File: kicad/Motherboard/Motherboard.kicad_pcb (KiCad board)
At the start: 2 copper layers, 72.1 x 0.1 mm, 68 parts, among them J1 USB_C_Receptacle_USB2.0, J10 Conn_01x08_Pin, J11 Conn_01x08_Pin, J12 Conn_01x08_Pin, J13 Conn_01x08_Pin, J2 Conn_01x02_Pin, J3 Conn_01x04_Pin, J4 Conn_01x04_Pin, J5 Conn_01x02_Pin, J6 Conn_01x08_Pin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

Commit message: Layout work
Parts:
- moved J8 96.0 mm to (154.9, 93.8), turned to -90 degrees
- moved J4 86.1 mm to (130.0, 129.8), turned to -90 degrees
- moved J10 84.0 mm to (86.2, 80.1), turned to 90 degrees
- moved J3 80.9 mm to (117.2, 129.8), turned to -90 degrees
- moved TP3 72.8 mm to (138.2, 107.6), turned to 180 degrees
- moved J5 66.6 mm to (90.0, 128.1), turned to -90 degrees
- moved J1 64.7 mm to (88.2, 119.8), turned to -90 degrees
- moved J2 56.5 mm to (103.7, 121.7), turned to 180 degrees
- moved Q1 56.4 mm to (95.7, 128.3), turned to 180 degrees
- moved J9 52.3 mm to (137.1, 80.0), turned to 90 degrees
- moved U6 50.6 mm to (144.4, 105.8), turned to 90 degrees
- moved R4 50.5 mm to (99.1, 128.1), turned to -90 degrees
- moved R1 50.3 mm to (96.0, 121.5), turned to 180 degrees
- moved R3 48.8 mm to (96.0, 118.5), turned to 0 degrees
- moved R5 42.8 mm to (103.9, 127.1), turned to 180 degrees
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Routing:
- net +3.3V: track 0.00 -> 55.6 mm
- net VS_1: track 0.00 -> 51.8 mm, vias 0 -> 2
- net Net-(U1-EN): track 0.00 -> 27.5 mm
- net Net-(J11-Pin_1): track 0.00 -> 10.7 mm
- net Net-(J11-Pin_8): track 0.00 -> 10.6 mm
- net Net-(J10-Pin_8): track 0.00 -> 9.72 mm
- net Net-(J10-Pin_1): track 0.00 -> 9.33 mm
- net Net-(J11-Pin_7): track 0.00 -> 8.74 mm
- net Net-(J11-Pin_2): track 0.00 -> 8.65 mm
- net Net-(J10-Pin_7): track 0.00 -> 8.04 mm
- net Net-(J10-Pin_2): track 0.00 -> 7.27 mm
- net Net-(J11-Pin_3): track 0.00 -> 7.10 mm
- net Net-(J11-Pin_6): track 0.00 -> 6.91 mm
- net Net-(J10-Pin_6): track 0.00 -> 6.30 mm
- net Net-(J11-Pin_4): track 0.00 -> 6.26 mm
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- added copper zone on B.Cu, net GND
- added copper zone on F.Cu, net GND
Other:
- board size 72.1 x 0.1 mm -> 72.6 x 54.1 mm

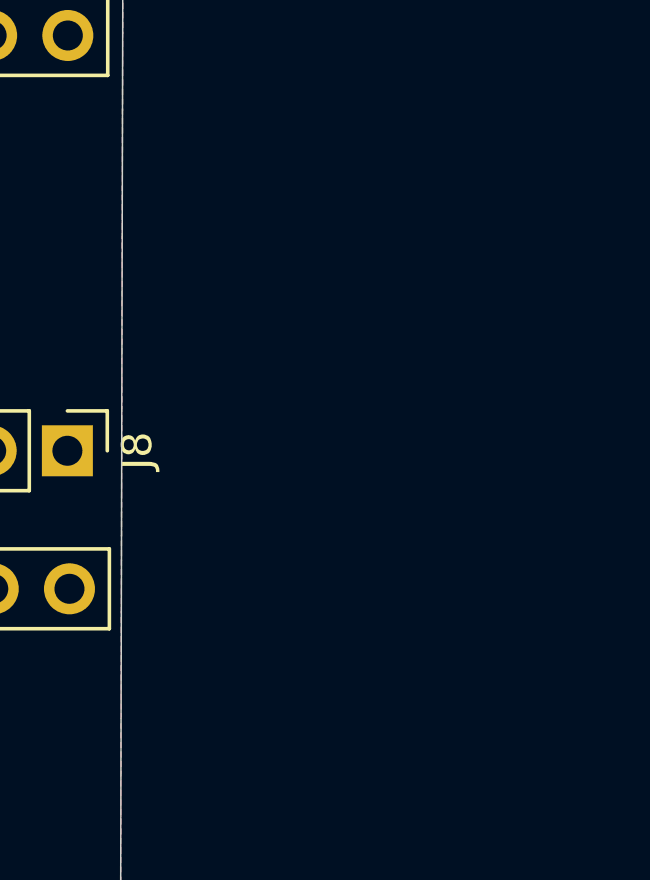
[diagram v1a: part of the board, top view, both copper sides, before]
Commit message: finalized schematic
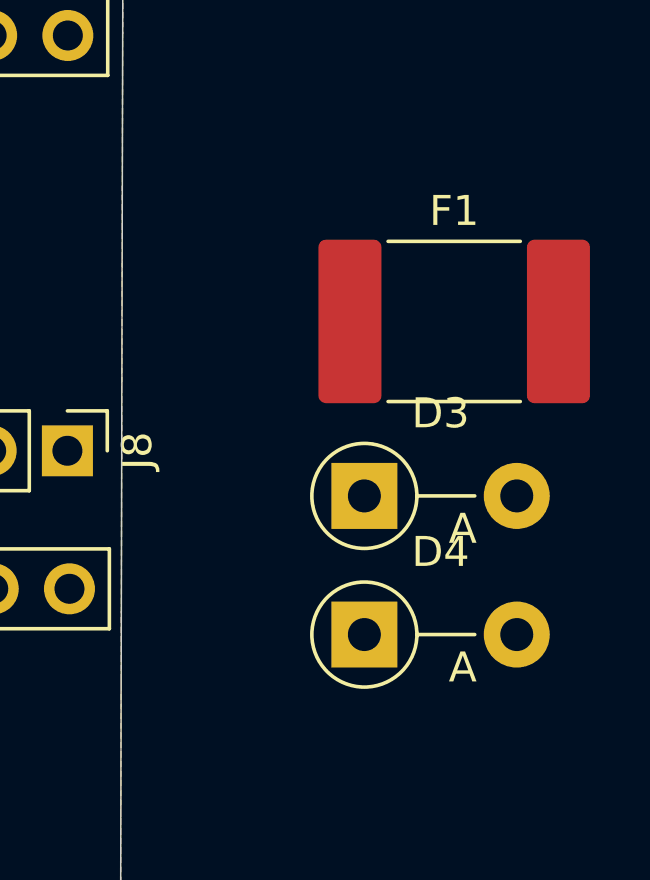
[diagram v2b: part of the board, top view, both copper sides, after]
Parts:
- added D3: 1N5819, Diode_THT:D_DO-41_SOD81_P5.08mm_Vertical_AnodeUp, F.Cu at (164.8, 95.3)
- added D4: 1N5819, Diode_THT:D_DO-41_SOD81_P5.08mm_Vertical_AnodeUp, F.Cu at (164.8, 100.0)
- added F1: Polyfuse, Fuse:Fuse_2920_7451Metric_Pad2.10x5.45mm_HandSolder, F.Cu at (167.8, 89.5)
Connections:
- C8 pad 1: +5V -> Net-(D4-A)
- J1 pad A4: +5V -> Net-(D3-A)
- J1 pad A9: +5V -> Net-(D3-A)
- J1 pad B4: +5V -> Net-(D3-A)
- J1 pad B9: +5V -> Net-(D3-A)
- L1 pad 2: +5V -> Net-(D4-A)
- TP2 pad 1: +5V -> Net-(D4-A)

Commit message: finish pls sia
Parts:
- moved F1 80.6 mm to (89.5, 108.8)
- moved D3 69.0 mm to (99.9, 119.1), turned to -90 degrees
- moved D4 62.0 mm to (107.6, 124.0), turned to 90 degrees
- moved TP4 16.2 mm to (135.6, 118.6)
- moved J5 13.6 mm to (89.8, 114.6), turned to 90 degrees
- moved C3 13.3 mm to (99.7, 105.7), turned to 0 degrees
- moved L1 12.3 mm to (87.8, 97.9), turned to 0 degrees
- moved TP2 9.88 mm to (104.4, 114.9)
- moved U9 8.39 mm to (86.9, 103.6), turned to 0 degrees
- moved TP1 8.27 mm to (86.4, 113.5)
- moved R5 7.81 mm to (96.4, 129.3)
- moved J2 6.80 mm to (105.3, 128.3), turned to 90 degrees
- moved Q1 4.99 mm to (100.7, 128.3), turned to 0 degrees
- moved C8 4.68 mm to (93.8, 97.9)
- moved D2 3.84 mm to (103.8, 119.1)
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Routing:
- net +3.3V: track 55.6 -> 0.00 mm
- net +5V: track 0.00 -> 45.6 mm
- net Net-(U1-EN): track 27.5 -> 0.00 mm
- net Net-(J11-Pin_1): track 10.7 -> 0.00 mm
- net Net-(J11-Pin_8): track 10.6 -> 0.00 mm
- net Net-(J10-Pin_8): track 9.72 -> 0.00 mm
- net Net-(J10-Pin_1): track 9.33 -> 0.00 mm
- net Net-(J11-Pin_7): track 8.74 -> 0.00 mm
- net Net-(J5-Pin_1): track 0.00 -> 8.67 mm
- net Net-(J11-Pin_2): track 8.65 -> 0.00 mm
- net Net-(J10-Pin_7): track 8.04 -> 0.00 mm
- net Net-(J10-Pin_2): track 7.27 -> 0.00 mm
- net Net-(J11-Pin_3): track 7.10 -> 0.00 mm
- net Net-(J11-Pin_6): track 6.91 -> 0.00 mm
- net Net-(J10-Pin_6): track 6.30 -> 0.00 mm
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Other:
- board size 72.6 x 54.1 mm -> 73 x 52.6 mm

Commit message: finalized schematic
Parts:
- added D5: 1N5819, Diode_THT:D_DO-41_SOD81_P5.08mm_Vertical_AnodeUp, F.Cu at (161.4, 104.5)
- U7, U8: value TMC2208-LA -> TMC2209-LA
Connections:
- F1 pad 2: VS_1 -> Net-(D5-A)
- TP2 pad 1: Net-(D4-A) -> +5V

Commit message: Separated parts
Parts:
- moved D5 103.0 mm to (62.5, 133.5), turned to 90 degrees
- moved TP3 58.4 mm to (195.8, 97.3)
- moved J8 48.2 mm to (200.7, 78.2)
- moved J9 48.2 mm to (182.9, 65.0)
- moved U4 48.2 mm to (190.3, 71.4)
- moved J7 46.5 mm to (183.1, 120.9)
- moved U3 46.5 mm to (190.1, 127.9)
- moved J6 46.5 mm to (200.7, 133.8)
- moved J10 46.4 mm to (43.4, 62.1)
- moved J11 46.4 mm to (61.1, 75.9)
- moved R2 46.4 mm to (62.7, 71.9)
- moved SW1 46.4 mm to (62.7, 67.1)
- moved U5 46.4 mm to (52.2, 68.9)
- moved U6 45.8 mm to (190.0, 100.0)
- moved J12 45.8 mm to (200.3, 106.4)
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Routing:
- net VS_1: track 54.8 -> 0.00 mm, vias 2 -> 0
- net +5V: track 45.6 -> 0.00 mm
- net Net-(J5-Pin_1): track 8.67 -> 0.00 mm
- removed copper zone on B.Cu, net GND
- removed copper zone on F.Cu, net GND
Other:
- board outline removed

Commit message: sai please
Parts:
- moved TP5 75.2 mm to (149.7, 154.3)
- moved SW1 47.1 mm to (107.8, 80.6), turned to -90 degrees
- moved L1 29.3 mm to (77.4, 129.9)
- moved C8 26.5 mm to (82.3, 126.7)
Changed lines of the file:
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@@
 	(footprint "Capacitor_SMD:C_1210_3225Metric_Pad1.33x2.70mm_HandSolder"
 		(layer "F.Cu")
-		(at 60.1595 112.141)
+		(at 82.296 126.746)
 		(descr "Capacitor SMD 1210 (3225 Metric), square (rectangular) end terminal, IPC_7351 nominal with elongated pad for handsoldering. (Body size source: IPC-SM-782 page 76, https://www.pcb-3d.com/wordpress/wp-content/uploads/ipc-sm-782a_amendment_1_and_2.pdf), generated with kicad-footprint-generator")
 		(tags "capacitor handsolder")
@@
 	(footprint "Button_Switch_SMD:SW_Push_SPST_NO_Alps_SKRK"
 		(layer "F.Cu")
-		(at 62.6575 67.0925)
+		(at 107.823 80.577 -90)
 		(descr "http://www.alps.com/prod/info/E/HTML/Tact/SurfaceMount/SKRK/SKRKAHE020.html")
 		(tags "SMD SMT button")
 		(property "Reference" "SW1"
-			(at 0 -2.25 0)
+			(at 0 -2.25 90)
 			(layer "F.SilkS")
 			(effects
@@
 		)
 		(property "Value" "Reset"
-			(at 0 2.5 0)
+			(at 0 2.5 90)
 			(layer "F.Fab")
 			(effects
@@
 		)
 		(property "Footprint" "Button_Switch_SMD:SW_Push_SPST_NO_Alps_SKRK"
-			(at 0 0 0)
+			(at 0 0 -90)
 			(unlocked yes)
 			(layer "F.Fab")
@@
 		)
 		(property "Datasheet" "https://omronfs.omron.com/en_US/ecb/products/pdf/en-b3fs.pdf"
-			(at 0 0 0)
+			(at 0 0 -90)
 			(unlocked yes)
 			(layer "F.Fab")
@@
 		)
 		(property "Description" ""
-			(at 0 0 0)
+			(at 0 0 -90)
 			(unlocked yes)
 			(layer "F.Fab")
@@
 		(attr smd)
 		(fp_line
-			(start -2.07 -1.57)
-			(end 2.07 -1.57)
+			(start -2.07 1.57)
+			(end -2.07 1.27)
 			(stroke
 				(width 0.12)
@@
 		)
 		(fp_line
-			(start -2.07 -1.27)
-			(end -2.07 -1.57)
+			(start 2.07 1.57)
+			(end -2.07 1.57)
 			(stroke
 				(width 0.12)
@@
 		)
 		(fp_line
-			(start -2.07 1.57)
-			(end -2.07 1.27)
+			(start 2.07 1.27)
+			(end 2.07 1.57)
 			(stroke
 				(width 0.12)
@@
 		)
 		(fp_line
-			(start 2.07 -1.57)
-			(end 2.07 -1.27)
+			(start -2.07 -1.27)
+			(end -2.07 -1.57)
 			(stroke
 				(width 0.12)
@@
 		)
 		(fp_line
-			(start 2.07 1.27)
-			(end 2.07 1.57)
+			(start -2.07 -1.57)
+			(end 2.07 -1.57)
 			(stroke
 				(width 0.12)
@@
 		)
 		(fp_line
-			(start 2.07 1.57)
-			(end -2.07 1.57)
+			(start 2.07 -1.57)
+			(end 2.07 -1.27)
 			(stroke
 				(width 0.12)
@@
 		)
 		(fp_line
-			(start -2.75 -1.7)
-			(end 2.75 -1.7)
+			(start -2.75 1.7)
+			(end -2.75 -1.7)
 			(stroke
 				(width 0.05)
@@
 		)
 		(fp_line
-			(start -2.75 1.7)
-			(end -2.75 -1.7)
+			(start 2.75 1.7)
+			(end -2.75 1.7)
 			(stroke
 				(width 0.05)
@@
 		)
 		(fp_line
-			(start 2.75 -1.7)
-			(end 2.75 1.7)
+			(start -2.75 -1.7)
+			(end 2.75 -1.7)
 			(stroke
 				(width 0.05)
@@
 		)
 		(fp_line
-			(start 2.75 1.7)
-			(end -2.75 1.7)
+			(start 2.75 -1.7)
+			(end 2.75 1.7)
 			(stroke
 				(width 0.05)
@@
 		)
 		(fp_line
-			(start -1.95 -1.45)
-			(end 1.95 -1.45)
+			(start -1.95 1.45)
+			(end -1.95 -1.45)
 			(stroke
 				(width 0.1)
@@
 		)
 		(fp_line
-			(start -1.95 1.45)
-			(end -1.95 -1.45)
+			(start 1.95 1.45)
+			(end -1.95 1.45)
 			(stroke
 				(width 0.1)
@@
 		)
 		(fp_line
-			(start 1.95 -1.45)
-			(end 1.95 1.45)
+			(start -1.95 -1.45)
+			(end 1.95 -1.45)
 			(stroke
 				(width 0.1)
@@
 		)
 		(fp_line
-			(start 1.95 1.45)
-			(end -1.95 1.45)
+			(start 1.95 -1.45)
+			(end 1.95 1.45)
 			(stroke
 				(width 0.1)
@@
 		)
 		(fp_text user "${REFERENCE}"
-			(at 0 0 0)
+			(at 0 0 90)
 			(layer "F.Fab")
 			(effects
@@
 		)
 		(pad "1" smd roundrect
-			(at -2.1 0)
+			(at -2.1 0 270)
 			(size 0.8 2)
 			(layers "F.Cu" "F.Paste" "F.Mask")
@@
 		)
 		(pad "2" smd roundrect
-			(at 2.1 0)
+			(at 2.1 0 270)
 			(size 0.8 2)
 			(layers "F.Cu" "F.Paste" "F.Mask")
@@
 	(footprint "Inductor_SMD:L_1008_2520Metric_Pad1.43x2.20mm_HandSolder"
 		(layer "F.Cu")
-		(at 54.1215 112.141)
+		(at 77.3625 129.921)
 		(descr "Inductor SMD 1008 (2520 Metric), square (rectangular) end terminal, IPC_7351 nominal with elongated pad for handsoldering. (Body size source: https://ecsxtal.com/store/pdf/ECS-MPI2520-SMD-POWER-INDUCTOR.pdf), generated with kicad-footprint-generator")
 		(tags "inductor handsolder")
@@
 	(footprint "TestPoint:TestPoint_Pad_1.5x1.5mm"
 		(layer "F.Cu")
-		(at 132.334 81.153)
+		(at 149.733 154.305)
 		(descr "SMD rectangular pad as test Point, square 1.5mm side length")
 		(tags "test point SMD pad rectangle square")

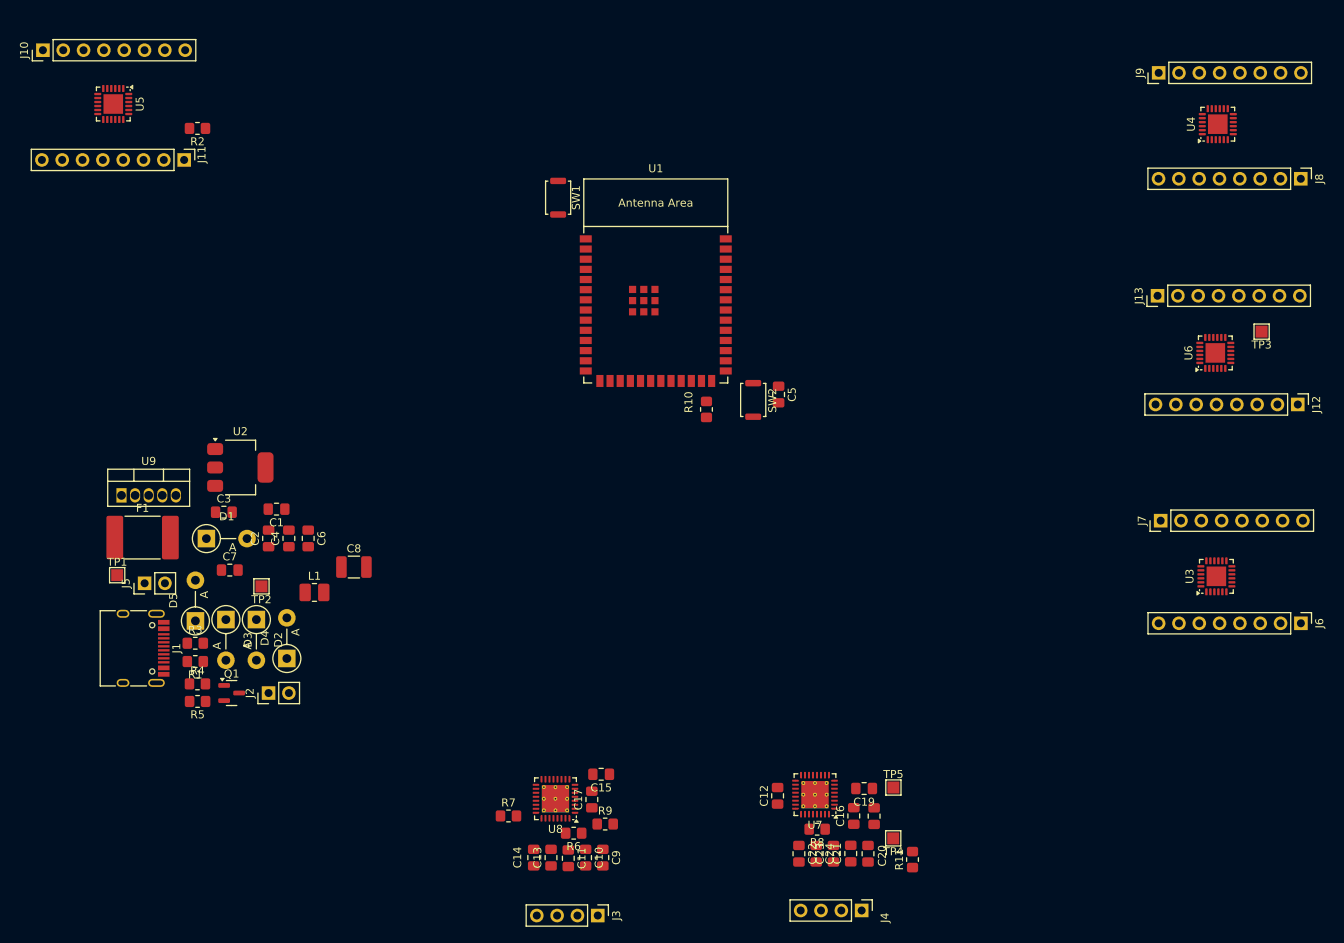
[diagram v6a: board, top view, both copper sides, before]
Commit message: updated layout
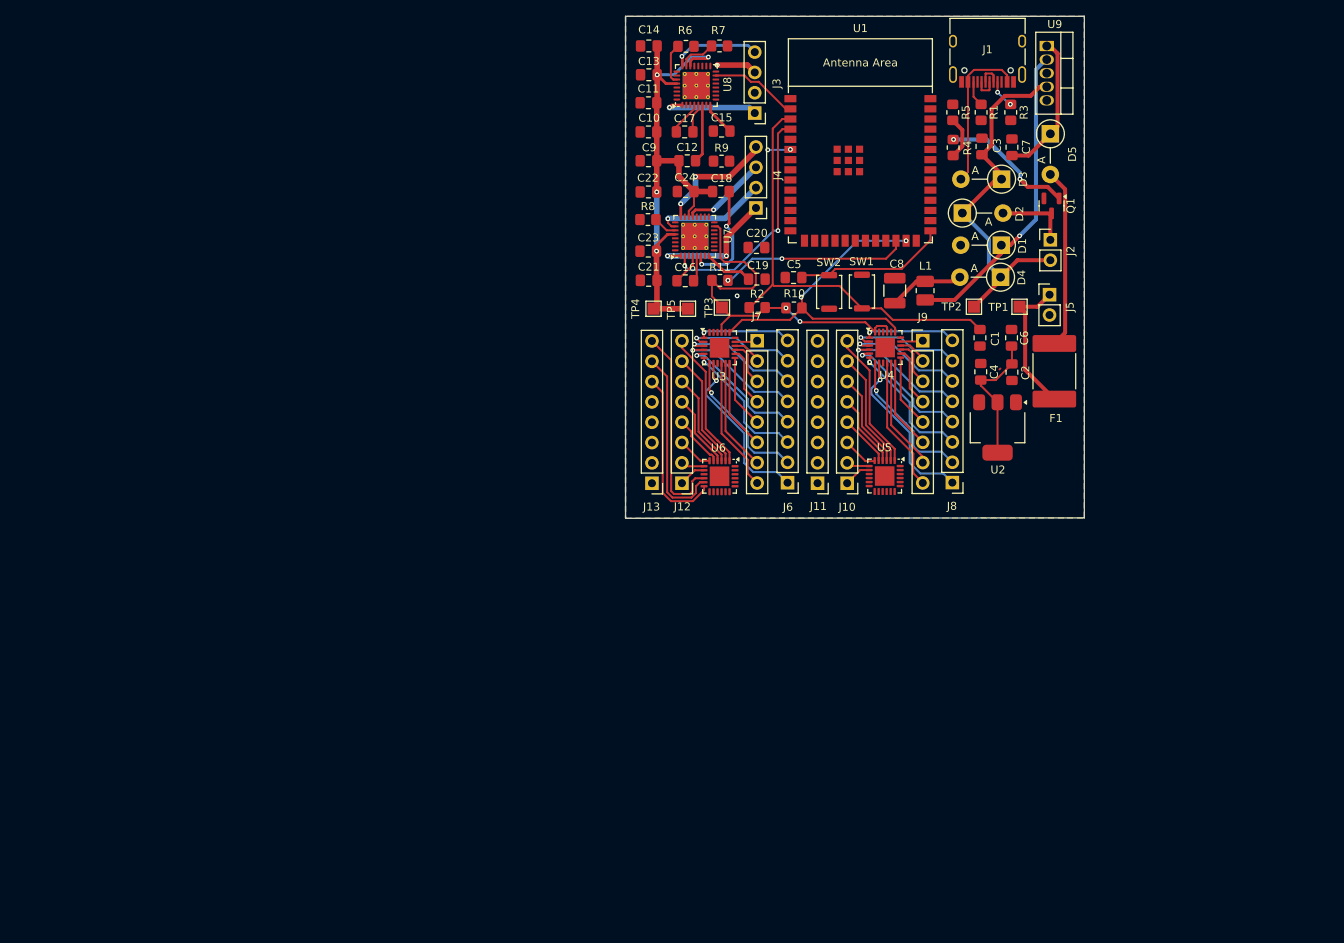
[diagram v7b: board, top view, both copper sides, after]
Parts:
- moved J1 130.6 mm to (161.5, 62.1), turned to 180 degrees
- moved U9 128.6 mm to (168.9, 61.6), turned to -90 degrees
- moved D5 123.0 mm to (169.3, 72.6), turned to -90 degrees
- moved R3 121.6 mm to (164.4, 69.9), turned to -90 degrees
- moved R1 119.8 mm to (160.7, 69.9), turned to 90 degrees
- moved R5 119.7 mm to (157.2, 69.9), turned to -90 degrees
- moved Q1 119.2 mm to (169.5, 81.6), turned to -90 degrees
- moved J5 118.7 mm to (169.2, 92.7), turned to 0 degrees
- moved TP1 117.7 mm to (165.5, 94.2), turned to -90 degrees
- moved F1 115.9 mm to (169.8, 102.3), turned to 90 degrees
- moved R4 115.8 mm to (157.2, 74.3), turned to 90 degrees
- moved J10 114.2 mm to (143.9, 116.3), turned to 180 degrees
- moved J2 113.0 mm to (169.3, 85.8), turned to 0 degrees
- moved D3 111.5 mm to (163.2, 78.3), turned to 180 degrees
- moved C7 111.1 mm to (164.6, 74.3), turned to 90 degrees
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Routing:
- net VS_1: track 0.00 -> 85.5 mm, vias 0 -> 4
- net +3.3V: track 0.00 -> 75.8 mm, vias 0 -> 2
- net Net-(U1-EN): track 0.00 -> 54.6 mm
- net +5V: track 0.00 -> 47.1 mm
- net SCL: track 0.00 -> 41.0 mm, vias 0 -> 2
- net Net-(D1-K): track 0.00 -> 39.2 mm, vias 0 -> 1
- net ENN_2: track 0.00 -> 29.1 mm, vias 0 -> 2
- net Net-(J13-Pin_8): track 0.00 -> 25.6 mm
- net SDA: track 0.00 -> 23.6 mm, vias 0 -> 2
- net Net-(J13-Pin_7): track 0.00 -> 23.3 mm
- net Net-(D5-A): track 0.00 -> 22.5 mm
- net Net-(J6-Pin_1): track 0.00 -> 21.5 mm, vias 0 -> 1
- net Net-(J8-Pin_1): track 0.00 -> 21.3 mm, vias 0 -> 1
- net Net-(J13-Pin_6): track 0.00 -> 21.1 mm
- net Net-(D3-A): track 0.00 -> 19.6 mm
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- added copper zone on B.Cu, net GND
- added copper zone on F.Cu, net GND
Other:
- board outline added: 57.3 x 62.8 mm
- board text added: "C18"
